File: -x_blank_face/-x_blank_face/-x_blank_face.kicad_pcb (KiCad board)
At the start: 2 copper layers, 87 x 326.5 mm, 18 parts

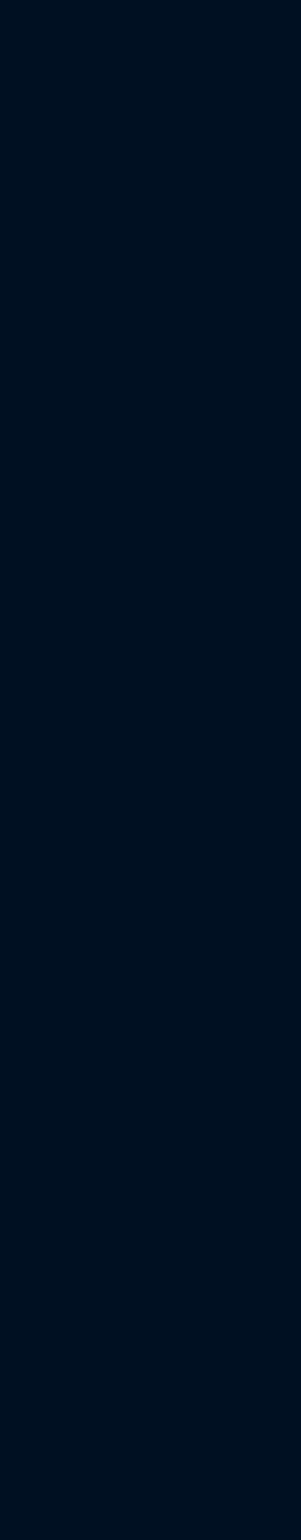
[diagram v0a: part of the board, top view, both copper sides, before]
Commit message: Changes solar panels
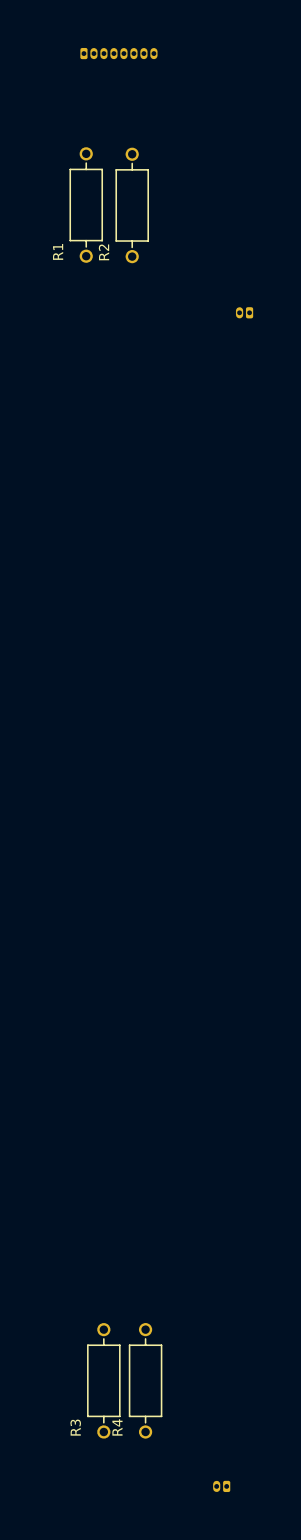
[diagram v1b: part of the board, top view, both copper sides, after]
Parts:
- added J1: Conn_01x08_Pin, CNN_GNSS_Footprint:DF13-8P, B.Cu at (114.5, -38.6)
- added J2: Conn_01x02_Pin, CNN_GNSS_Footprint:DF13-2P, B.Cu at (130.1, -1.11)
- added J2: Conn_01x02_Pin, CNN_GNSS_Footprint:DF13-2P, B.Cu at (127.3, 145.7)
- added R1: 75, CNN_GNSS_Footprint:UB3C-75RF1, F.Cu at (110.8, -13.8)
- added R2: 75, CNN_GNSS_Footprint:UB3C-75RF1, F.Cu at (116.5, -13.8)
- added R3: 75, CNN_GNSS_Footprint:UB3C-75RF1, F.Cu at (113.0, 133.2)
- added R4: 75, CNN_GNSS_Footprint:UB3C-75RF1, F.Cu at (118.2, 133.2)

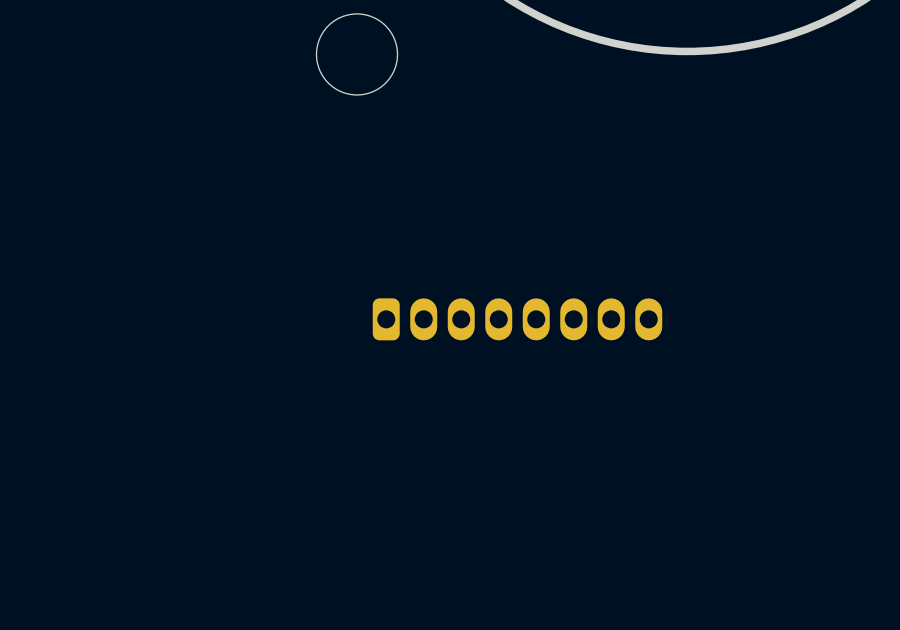
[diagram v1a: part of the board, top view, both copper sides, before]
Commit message: added schematic to +x and routed ish the schematic
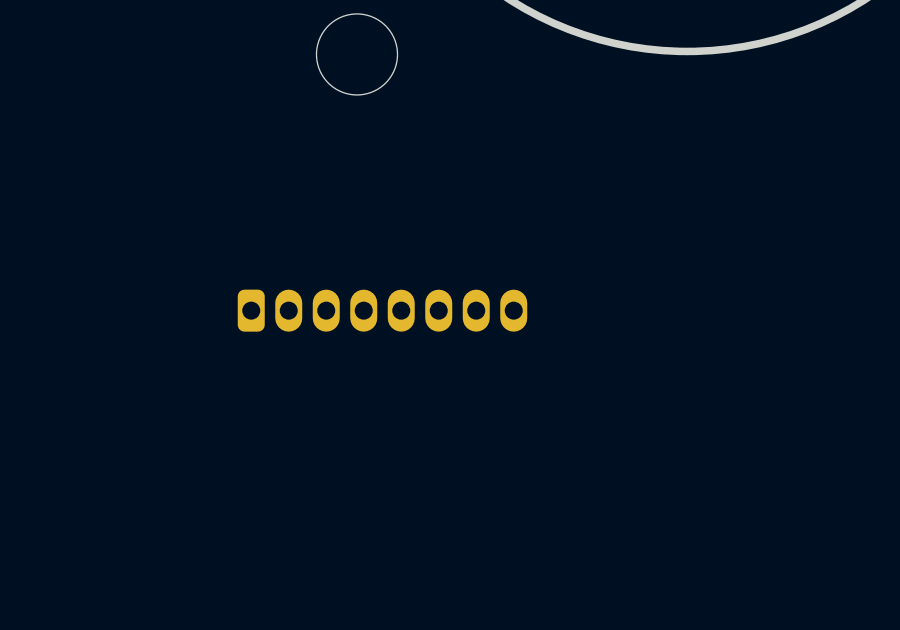
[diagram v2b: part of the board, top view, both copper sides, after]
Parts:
- moved J1 4.51 mm to (110.0, -38.9)
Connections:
- R1 pad 2: GND -> /+X Drain
- R2 pad 2: GND -> /+X Drain
- R3 pad 2: GND -> /+X Drain
- R4 pad 2: GND -> /+X Drain
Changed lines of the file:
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@@
 			(layers "*.Cu" "*.Mask")
 			(remove_unused_layers no)
-			(net 1 "GND")
+			(net 2 "/+X Drain")
 			(pintype "passive")
 		)
@@
 			(layers "*.Cu" "*.Mask")
 			(remove_unused_layers no)
-			(net 1 "GND")
+			(net 2 "/+X Drain")
 			(pintype "passive")
 		)
@@
 			(layers "*.Cu" "*.Mask")
 			(remove_unused_layers no)
-			(net 1 "GND")
+			(net 2 "/+X Drain")
 			(pintype "passive")
 		)
@@
 			(layers "*.Cu" "*.Mask")
 			(remove_unused_layers no)
-			(net 1 "GND")
+			(net 2 "/+X Drain")
 			(pintype "passive")
 		)
@@
 	(footprint "CNN_GNSS_Footprint:DF13-8P"
 		(layer "B.Cu")
-		(at 114.52 -38.62)
+		(at 110.02 -38.91)
 		(property "Reference" "J1"
 			(at 0.505 -3.6 180)
@@
 		)
 	)
+	(dimension
+		(type orthogonal)
+		(layer "Dwgs.User")
+		(pts
+			(xy 77.5 -40.05) (xy 77.5 -44.1)
+		)
+		(height 3.01)
+		(orientation 1)
+		(format
+			(prefix "")
+			(suffix "")
+			(units 3)
+			(units_format 0)
+			(precision 4)
+			(suppress_zeroes yes)
+		)
+		(style
+			(thickness 0.1)
+			(arrow_length 1.27)
+			(text_position_mode 0)
+			(arrow_direction outward)
+			(extension_height 0.58642)
+			(extension_offset 0.5)
+			(keep_text_aligned yes)
+		)
+		(gr_text "4.05"
+			(at 79.36 -42.075 90)
+			(layer "Dwgs.User")
+			(effects
+				(font
+					(size 1 1)
+					(thickness 0.15)
+				)
+			)
+		)
+	)

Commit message: changed switch connector footprint
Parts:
- removed the J2 at (127.3, 145.7)
- added J3: Conn_01x02_Pin, CNN_GNSS_Footprint:CON2_1X2_UR_DF13, B.Cu at (113.6, 162.3)
- J2: footprint CNN_GNSS_Footprint:DF13-2P -> CNN_GNSS_Footprint:CON2_1X2_UR_DF13
- moved J1 1.87 mm to (110.1, -37.0)
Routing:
- added copper zone on B.Cu, net /+X Drain
- added copper zone on F.Cu, net /12VPDM
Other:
- board size 87 x 326.5 mm -> 276.2 x 353.8 mm
- board text added: "For Instructional Use Only."
- board text added: "SOLIDWORKS Educational Product."

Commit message: Updated panels based on dxf drawings from mech, need to move all holes up 5mm
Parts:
- added Sepic1: ~, Connection_Pads:DF13_Horizontal, B.Cu at (87.4, -49.4)
- moved R1 25.0 mm to (134.9, -7.58)
- moved J3 22.2 mm to (132.7, 151.2)
- moved R3 18.0 mm to (130.7, 130.0)
- moved R4 17.0 mm to (134.9, 130.0)
- moved R2 15.5 mm to (130.7, -7.60)
- moved J2 14.2 mm to (133.2, 12.8)
- moved H5 6.50 mm to (150.1, 35.9)
- moved H10 6.48 mm to (74.0, 35.9)
- moved J1 1.56 mm to (111.6, -37.6)
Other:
- board size 276.2 x 353.8 mm -> 87 x 326.5 mm
- board text added: "${REFERENCE}"
- board text removed: "For Instructional Use Only."
- board text removed: "SOLIDWORKS Educational Product."

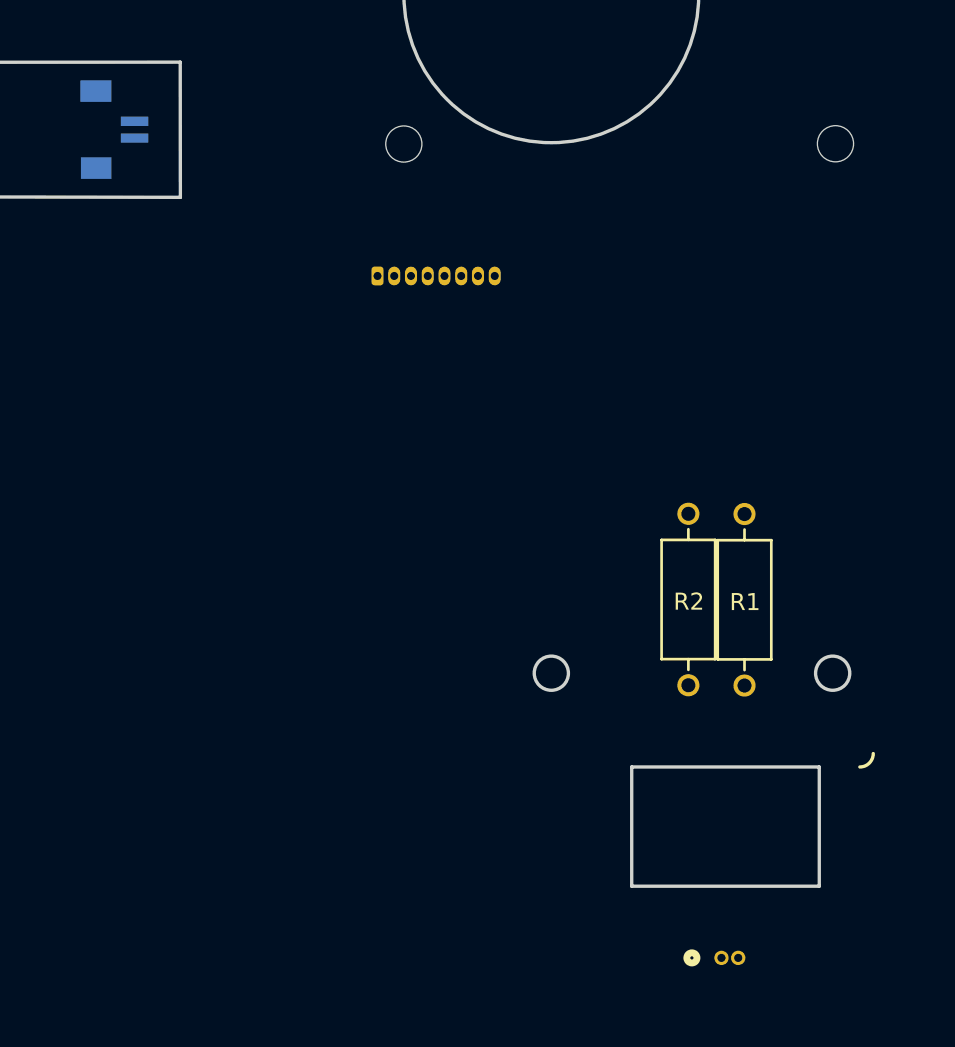
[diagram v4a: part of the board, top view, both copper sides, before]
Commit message: moved holes up 5mm, did what Jack said to do
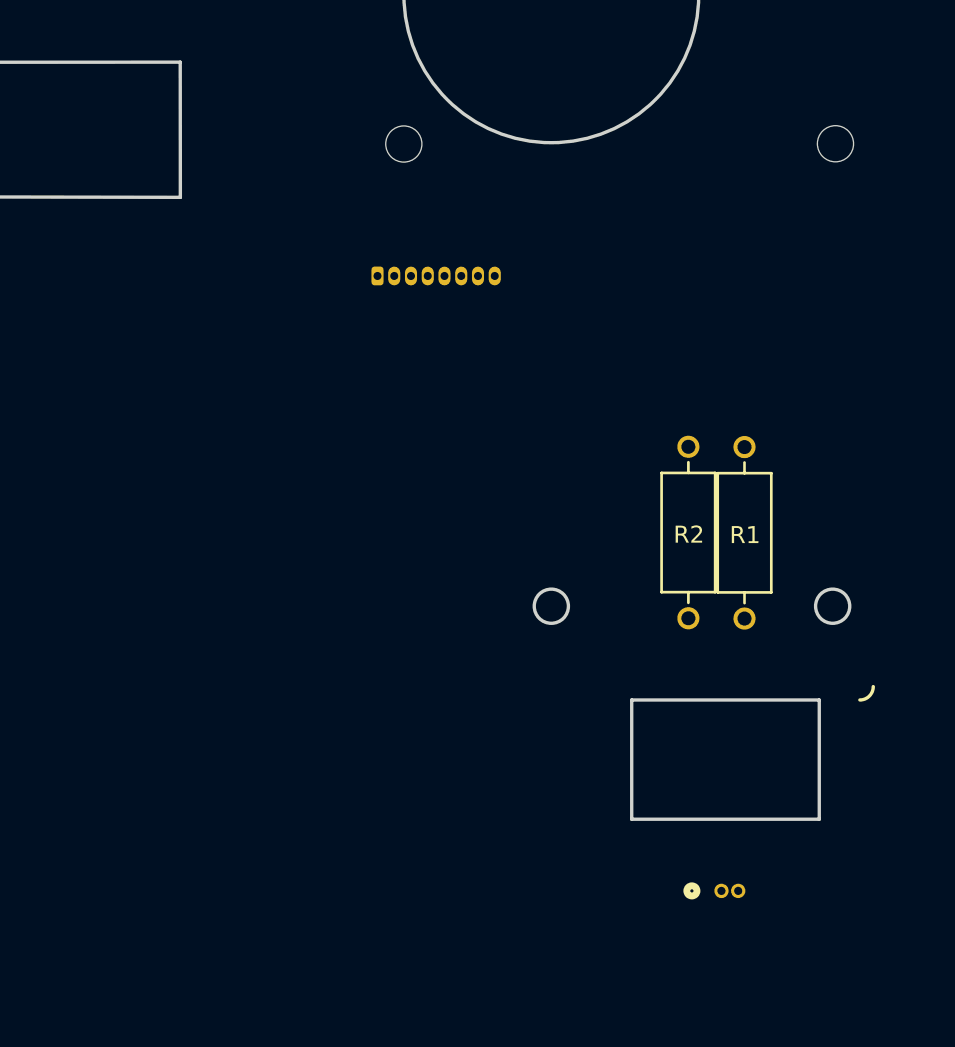
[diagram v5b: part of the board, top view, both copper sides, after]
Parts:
- removed Sepic1: ~, Connection_Pads:DF13_Horizontal
- moved R1 5.00 mm to (134.9, -12.6)
- moved J2 5.00 mm to (133.2, 7.75)
- moved R2 5.00 mm to (130.7, -12.6)
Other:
- outline, holes or cut-outs redrawn

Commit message: Moved some things around, locked some components
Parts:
- added H19: MountingHole, CNN_GNSS_Footprint:2.55mm_Mounting_Hole, F.Cu at (120.5, -13.6)
- added H20: MountingHole, CNN_GNSS_Footprint:2.55mm_Mounting_Hole, F.Cu at (141.5, -13.6)
- added H21: MountingHole, CNN_GNSS_Footprint:2.55mm_Mounting_Hole, F.Cu at (120.5, 129.4)
- added H22: MountingHole, CNN_GNSS_Footprint:2.55mm_Mounting_Hole, F.Cu at (141.5, 129.4)
- moved J2 5.70 mm to (134.4, 13.3), turned to 0 degrees
- moved J3 3.89 mm to (134.1, 154.8), turned to 0 degrees
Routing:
- net /-X Serial Out: track 0.00 -> 212.4 mm
- net GND: track 0.00 -> 212.2 mm
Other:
- outline, holes or cut-outs redrawn

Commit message: changed ALOT of things, got it to a point to send mech models,solar panel harness on BS need changed
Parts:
- moved J3 8.49 mm to (134.2, 163.3)
- moved J2 7.30 mm to (134.8, 20.6)
- moved J1 5.00 mm to (116.6, -37.6)
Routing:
- net GND: track 212.2 -> 220.8 mm
- net /-X Serial Out: track 212.4 -> 220.0 mm
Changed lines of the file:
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@@
 			(unlocked yes)
 			(layer "F.SilkS")
+			(hide yes)
 			(effects
 				(font
@@
 			(unlocked yes)
 			(layer "F.SilkS")
+			(hide yes)
 			(effects
 				(font
@@
 			(unlocked yes)
 			(layer "F.SilkS")
+			(hide yes)
 			(effects
 				(font
@@
 			(unlocked yes)
 			(layer "F.SilkS")
+			(hide yes)
 			(effects
 				(font
@@
 	(footprint "CNN_GNSS_Footprint:DF13-8P"
 		(layer "B.Cu")
-		(at 111.58 -37.6)
+		(at 116.58 -37.6)
 		(property "Reference" "J1"
 			(at 0.505 -3.6 180)
@@
 	(footprint "CNN_GNSS_Footprint:CON2_1X2_UR_DF13"
 		(layer "B.Cu")
-		(at 134.05 154.83)
+		(at 134.2016 163.3161)
 		(tags "DF13-2P-1.25DS20 ")
 		(property "Reference" "J3"
@@
 	(footprint "CNN_GNSS_Footprint:CON2_1X2_UR_DF13"
 		(layer "B.Cu")
-		(at 134.39 13.33)
+		(at 134.7616 20.6161)
 		(tags "DF13-2P-1.25DS20 ")
 		(property "Reference" "J2"
@@
 		)
 	)
+	(dimension
+		(type orthogonal)
+		(layer "Dwgs.User")
+		(pts
+			(xy 155.51 -39.15) (xy 116.91 -39.85)
+		)
+		(height 6.28)
+		(orientation 0)
+		(format
+			(prefix "")
+			(suffix "")
+			(units 3)
+			(units_format 0)
+			(precision 4)
+			(suppress_zeroes yes)
+		)
+		(style
+			(thickness 0.1)
+			(arrow_length 1.27)
+			(text_position_mode 0)
+			(arrow_direction outward)
+			(extension_height 0.58642)
+			(extension_offset 0.5)
+			(keep_text_aligned yes)
+		)
+		(gr_text "38.6"
+			(at 136.21 -34.02 0)
+			(layer "Dwgs.User")
+			(effects
+				(font
+					(size 1 1)
+					(thickness 0.15)
+				)
+			)
+		)
+	)
 	(segment
-		(start 146.22 25.16)
-		(end 134.39 13.33)
+		(start 146.22 32.09)
+		(end 134.7616 20.6316)
 		(width 0.2)
 		(layer "B.Cu")
@@
 	)
 	(segment
-		(start 133.77 12.705)
-		(end 114.415 -6.65)
+		(start 121.285 -38.15)
+		(end 117.936 -34.801)
 		(width 0.2)
 		(layer "B.Cu")
@@
 	)
 	(segment
-		(start 115.035 -38.15)
-		(end 116.285 -38.15)
+		(start 134.2016 163.3161)
+		(end 134.2016 155.2784)
 		(width 0.2)
 		(layer "B.Cu")
@@
 	)
 	(segment
-		(start 146.22 142.66)
-		(end 146.22 25.16)
+		(start 146.22 143.26)
+		(end 146.22 32.09)
 		(width 0.2)
 		(layer "B.Cu")
@@
 	)
 	(segment
-		(start 134.05 154.83)
-		(end 146.22 142.66)
+		(start 134.2016 155.2784)
+		(end 146.22 143.26)
 		(width 0.2)
 		(layer "B.Cu")
@@
 	)
 	(segment
-		(start 115.035 -6.025)
-		(end 115.035 -38.15)
+		(start 134.7616 20.6316)
+		(end 134.7616 20.6161)
 		(width 0.2)
 		(layer "B.Cu")
@@
 	)
 	(segment
-		(start 145.18 142.45)
-		(end 145.18 25.37)
+		(start 117.936 3.7905)
+		(end 134.7616 20.6161)
+		(width 0.2)
+		(layer "B.Cu")
+		(net 1)
+	)
+	(segment
+		(start 117.936 -34.801)
+		(end 117.936 3.7905)
+		(width 0.2)
+		(layer "B.Cu")
+		(net 1)
+	)
+	(segment
+		(start 121.285 -38.15)
+		(end 120.035 -38.15)
+		(width 0.2)
+		(layer "B.Cu")
+		(net 1)
+	)
+	(segment
+		(start 117.535 -38.15)
+		(end 118.785 -38.15)
+		(width 0.2)
+		(layer "B.Cu")
+		(net 3)
+	)
+	(segment
+		(start 133.5116 20.6161)
+		(end 145.18 32.2845)
+		(width 0.2)
+		(layer "B.Cu")
+		(net 3)
+	)
+	(segment
+		(start 116.840137 -36.82)
+		(end 116.840137 4.190137)
+		(width 0.2)
+		(layer "B.Cu")
+		(net 3)
+	)
+	(segment
+		(start 117.535 -37.514863)
+		(end 116.840137 -36.82)
 		(width 0.2)
 		(layer "B.Cu")
@@
 	)
 	(segment
-		(start 113.785 -38.15)
-		(end 112.535 -38.15)
+		(start 117.535 -38.15)
+		(end 117.535 -37.514863)
 		(width 0.2)
 		(layer "B.Cu")
@@
 	)
 	(segment
-		(start 133.77 13.955)
-		(end 114.415 -5.4)
+		(start 116.840137 4.190137)
+		(end 133.2661 20.6161)
 		(width 0.2)
 		(layer "B.Cu")
@@
 	)
 	(segment
-		(start 132.8 154.83)
+		(start 133.2661 20.6161)
+		(end 133.5116 20.6161)
+		(width 0.2)
+		(layer "B.Cu")
+		(net 3)
+	)
+	(segment
+		(start 132.9516 154.6784)
 		(end 145.18 142.45)
 		(width 0.2)
@@
 	)
 	(segment
-		(start 113.785 -6.025)
-		(end 113.785 -38.15)
+		(start 132.9516 163.3161)
+		(end 132.9516 154.6784)
 		(width 0.2)
 		(layer "B.Cu")
@@
 	)
 	(segment
-		(start 145.18 25.37)
-		(end 133.14 13.33)
+		(start 145.18 32.2845)
+		(end 145.18 142.45)
 		(width 0.2)
 		(layer "B.Cu")
@@
 		(polygon
 			(pts
-				(xy 68.39 -104.22) (xy 155.63 -104.22) (xy 155.64 222.53) (xy 68.38 222.53)
+				(xy 68.388089 -41.79) (xy 155.631911 -41.79) (xy 155.63722 131.68) (xy 68.38278 131.68)
 			)
 		)
@@
 		(polygon
 			(pts
-				(xy 68.459885 -104.192627) (xy 155.699885 -104.192627) (xy 155.709885 222.557373) (xy 68.449885 222.557373)
+				(xy 68.457975 -41.782627) (xy 155.701795 -41.782627) (xy 155.707104 131.687373) (xy 68.452666 131.687373)
 			)
 		)

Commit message: I forgot what I changed
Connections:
- J1 pad 1: /12VPDM -> GND
- J1 pad 2: /12VPDM -> GND
- J1 pad 3: /+X Drain -> /-X Serial Out
- J1 pad 4: /+X Drain -> /-X Serial Out
- J1 pad 5: /-X Serial Out -> /+X Drain
- J1 pad 6: /-X Serial Out -> /+X Drain
- J1 pad 7: GND -> /12VPDM
- J1 pad 8: GND -> /12VPDM
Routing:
- net /+X Drain: track 0.00 -> 1.89 mm
- net GND: track 220.8 -> 221.4 mm
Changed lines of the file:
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@@
 			(remove_unused_layers no)
 			(roundrect_rratio 0.25)
-			(net 4 "/12VPDM")
+			(net 1 "GND")
 			(pinfunction "Pin_1")
 			(pintype "passive")
@@
 			(layers "*.Cu" "*.Mask")
 			(remove_unused_layers no)
-			(net 4 "/12VPDM")
+			(net 1 "GND")
 			(pinfunction "Pin_2")
 			(pintype "passive")
@@
 			(layers "*.Cu" "*.Mask")
 			(remove_unused_layers no)
-			(net 2 "/+X Drain")
+			(net 3 "/-X Serial Out")
 			(pinfunction "Pin_3")
 			(pintype "passive")
@@
 			(layers "*.Cu" "*.Mask")
 			(remove_unused_layers no)
-			(net 2 "/+X Drain")
+			(net 3 "/-X Serial Out")
 			(pinfunction "Pin_4")
 			(pintype "passive")
@@
 			(layers "*.Cu" "*.Mask")
 			(remove_unused_layers no)
-			(net 3 "/-X Serial Out")
+			(net 2 "/+X Drain")
 			(pinfunction "Pin_5")
 			(pintype "passive")
@@
 			(layers "*.Cu" "*.Mask")
 			(remove_unused_layers no)
-			(net 3 "/-X Serial Out")
+			(net 2 "/+X Drain")
 			(pinfunction "Pin_6")
 			(pintype "passive")
@@
 			(layers "*.Cu" "*.Mask")
 			(remove_unused_layers no)
-			(net 1 "GND")
+			(net 4 "/12VPDM")
 			(pinfunction "Pin_7")
 			(pintype "passive")
@@
 			(layers "*.Cu" "*.Mask")
 			(remove_unused_layers no)
-			(net 1 "GND")
+			(net 4 "/12VPDM")
 			(pinfunction "Pin_8")
 			(pintype "passive")
@@
 		(end 134.7616 20.6316)
 		(width 0.2)
-		(layer "B.Cu")
-		(net 1)
-	)
-	(segment
-		(start 121.285 -38.15)
-		(end 117.936 -34.801)
-		(width 0.2)
-		(layer "B.Cu")
+		(layer "F.Cu")
 		(net 1)
 	)
@@
 		(end 134.2016 155.2784)
 		(width 0.2)
-		(layer "B.Cu")
+		(layer "F.Cu")
 		(net 1)
 	)
@@
 		(end 146.22 32.09)
 		(width 0.2)
-		(layer "B.Cu")
+		(layer "F.Cu")
 		(net 1)
 	)
@@
 		(end 146.22 143.26)
 		(width 0.2)
-		(layer "B.Cu")
+		(layer "F.Cu")
+		(net 1)
+	)
+	(segment
+		(start 113.785 -38.15)
+		(end 113.785 -0.3605)
+		(width 0.2)
+		(layer "F.Cu")
+		(net 1)
+	)
+	(segment
+		(start 113.785 -0.3605)
+		(end 134.7616 20.6161)
+		(width 0.2)
+		(layer "F.Cu")
 		(net 1)
 	)
@@
 	)
 	(segment
-		(start 117.936 3.7905)
-		(end 134.7616 20.6161)
+		(start 113.785 -38.15)
+		(end 113.785 -38.4)
 		(width 0.2)
 		(layer "B.Cu")
@@
 	)
 	(segment
-		(start 117.936 -34.801)
-		(end 117.936 3.7905)
+		(start 113.785 -38.15)
+		(end 112.535 -38.15)
 		(width 0.2)
 		(layer "B.Cu")
@@
 	)
 	(segment
-		(start 121.285 -38.15)
-		(end 120.035 -38.15)
-		(width 0.2)
-		(layer "B.Cu")
-		(net 1)
+		(start 118.785 -38.15)
+		(end 117.535 -38.15)
+		(width 0.2)
+		(layer "F.Cu")
+		(net 2)
 	)
 	(segment
 		(start 117.535 -38.15)
-		(end 118.785 -38.15)
+		(end 117.535 -37.514863)
+		(width 0.2)
+		(layer "B.Cu")
+		(net 2)
+	)
+	(segment
+		(start 116.285 3.635)
+		(end 133.2661 20.6161)
+		(width 0.2)
+		(layer "B.Cu")
+		(net 3)
+	)
+	(segment
+		(start 116.285 -38.15)
+		(end 116.285 3.635)
+		(width 0.2)
+		(layer "B.Cu")
+		(net 3)
+	)
+	(segment
+		(start 133.2661 20.6161)
+		(end 133.5116 20.6161)
+		(width 0.2)
+		(layer "B.Cu")
+		(net 3)
+	)
+	(segment
+		(start 116.285 -38.15)
+		(end 115.035 -38.15)
 		(width 0.2)
 		(layer "B.Cu")
@@
 		(start 133.5116 20.6161)
 		(end 145.18 32.2845)
-		(width 0.2)
-		(layer "B.Cu")
-		(net 3)
-	)
-	(segment
-		(start 116.840137 -36.82)
-		(end 116.840137 4.190137)
-		(width 0.2)
-		(layer "B.Cu")
-		(net 3)
-	)
-	(segment
-		(start 117.535 -37.514863)
-		(end 116.840137 -36.82)
-		(width 0.2)
-		(layer "B.Cu")
-		(net 3)
-	)
-	(segment
-		(start 117.535 -38.15)
-		(end 117.535 -37.514863)
-		(width 0.2)
-		(layer "B.Cu")
-		(net 3)
-	)
-	(segment
-		(start 116.840137 4.190137)
-		(end 133.2661 20.6161)
-		(width 0.2)
-		(layer "B.Cu")
-		(net 3)
-	)
-	(segment
-		(start 133.2661 20.6161)
-		(end 133.5116 20.6161)
 		(width 0.2)
 		(layer "B.Cu")
@@
 		(polygon
 			(pts
-				(xy 68.388089 -41.79) (xy 155.631911 -41.79) (xy 155.63722 131.68) (xy 68.38278 131.68)
+				(xy 68.388179 -44.73) (xy 155.631821 -44.73) (xy 155.63722 131.68) (xy 68.38278 131.68)
 			)
 		)
@@
 		(polygon
 			(pts
-				(xy 68.457975 -41.782627) (xy 155.701795 -41.782627) (xy 155.707104 131.687373) (xy 68.452666 131.687373)
-			)
-		)
+				(xy 68.458065 -44.722627) (xy 155.701705 -44.722627) (xy 155.707104 131.687373) (xy 68.452666 131.687373)
+			)
+		)
